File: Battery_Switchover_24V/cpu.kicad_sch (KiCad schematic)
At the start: 54 parts, among them J8 USB_C_Receptacle_USB2.0_14P, M1 Fan, Q1 NPN, SW1 SW_Push, U11 OPA2197xD, U3 LPC11U14FBD48-201, U4 L5973D, U6 AMS1117-3.3, Y1 12.000MHz

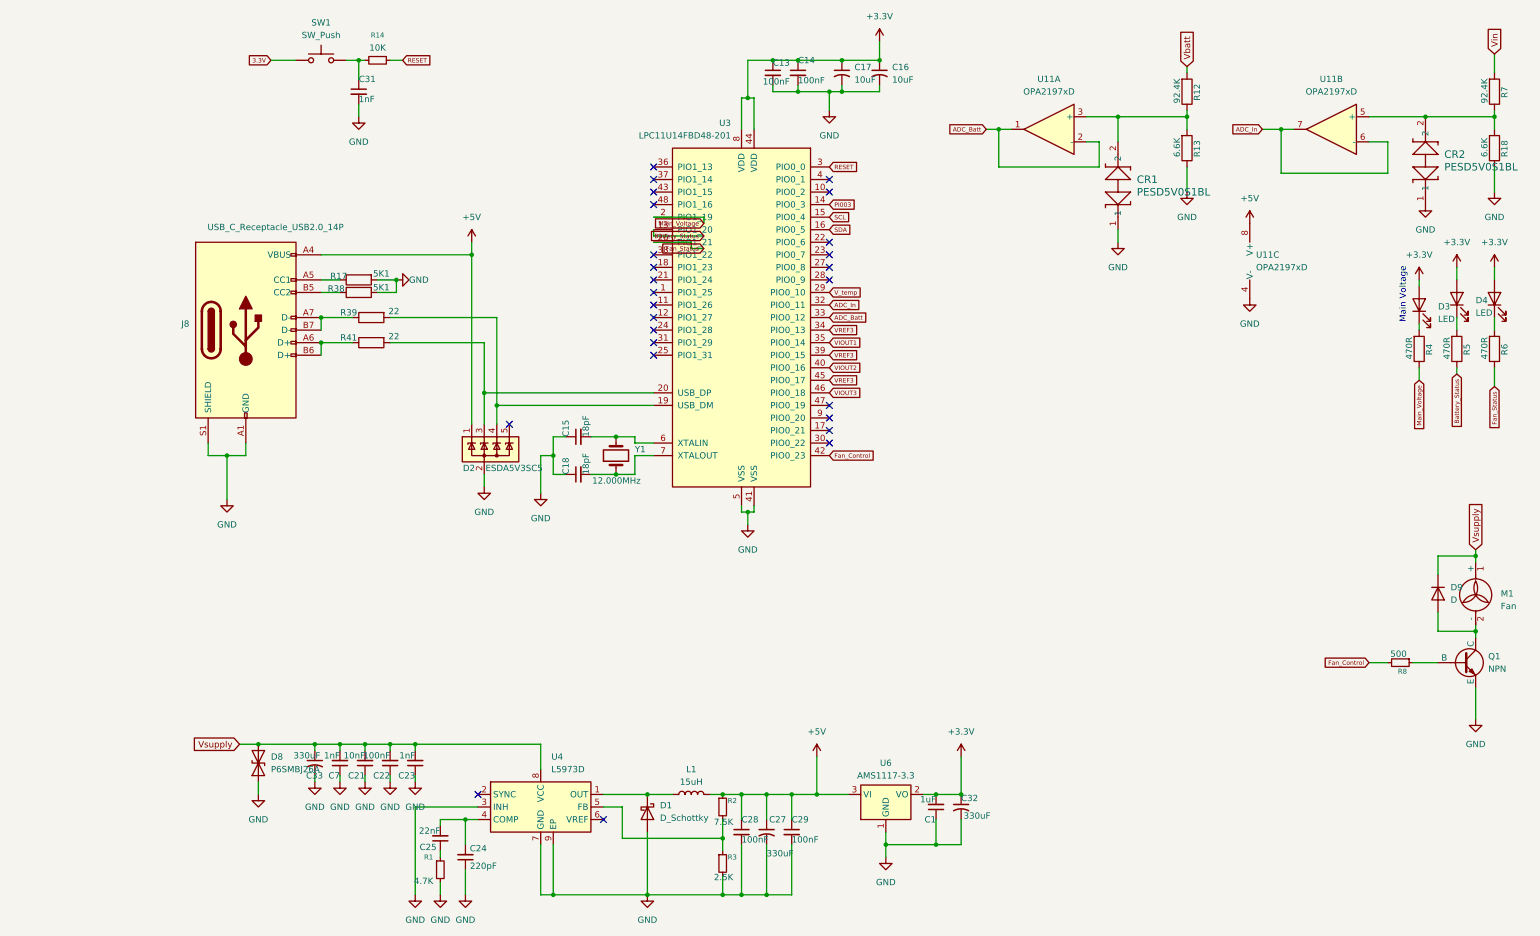
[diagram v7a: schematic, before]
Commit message: Added Some Footprints
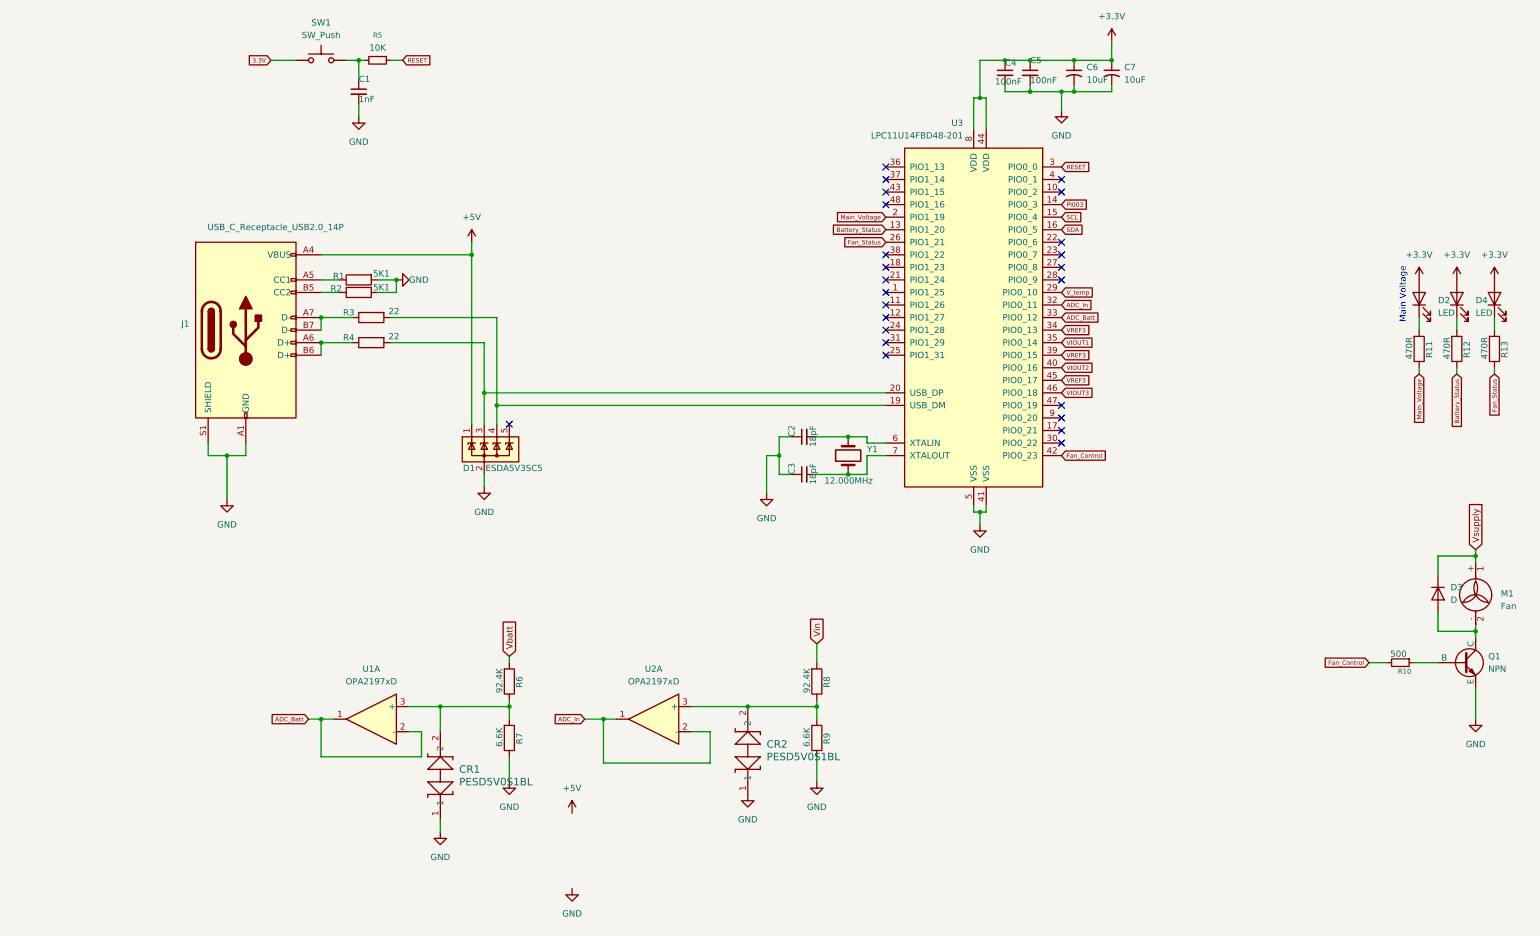
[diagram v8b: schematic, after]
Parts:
- removed C1: 1uF, symbol Device:C_Small
- removed C21: 10nF, symbol Device:C_Small
- removed C22, C28, C29: 100nF, symbol Device:C_Small
- removed C23, C7: 1nF, symbol Device:C_Small
- removed C24: 220pF, symbol Device:C_Small
- removed C25: 22nF, symbol Device:C_Small
- removed C27, C32, C33: 330uF, symbol Device:C_Small_US
- removed D1: D_Schottky, symbol Device:D_Schottky
- removed D8: P6SMBJ26A, symbol Device:D_TVS
- removed L1: 15uH, symbol Device:L
- removed R1: 4.7K, symbol Device:R_Small
- removed R2: 7.5K, symbol Device:R_Small
- removed R3: 2.5K, symbol Device:R_Small
- removed unit 3 of U11
- removed U4: L5973D, Package_SO:HSOP-8-1EP_3.9x4.9mm_P1.27mm_EP2.41x3.1mm_ThermalVias, symbol Regulator_Switching:L5973D
- removed U6: AMS1117-3.3, Package_TO_SOT_SMD:SOT-223-3_TabPin2, symbol Regulator_Linear:AMS1117-3.3
- C1: renamed from C31; footprint (none) -> Capacitor_SMD:C_0603_1608Metric
- C2: renamed from C15; footprint (none) -> Capacitor_SMD:C_0402_1005Metric
- C3: renamed from C18; footprint (none) -> Capacitor_SMD:C_0402_1005Metric
- C4: renamed from C13; footprint (none) -> Capacitor_SMD:C_0603_1608Metric
- C5: renamed from C14; footprint (none) -> Capacitor_SMD:C_0603_1608Metric
- R10: renamed from R8; footprint (none) -> Resistor_SMD:R_0603_1608Metric
- R5: renamed from R14; footprint (none) -> Resistor_SMD:R_0603_1608Metric
- Y1: footprint (none) -> Crystal:Crystal_SMD_HC49-SD
- renumbered C17 to C6, C16 to C7, D2 to D1, D3 to D2, D9 to D3, J8 to J1, R17 to R1, R4 to R11, R5 to R12, R6 to R13, R38 to R2, R39 to R3, R41 to R4, R12 to R6, R13 to R7, R7 to R8, R18 to R9, U11 to U1, U11 to U2
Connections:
- net ADC_In: now also U2.1, U2.2 (-); no longer U2.6 (-), U2.7
- net at CR2.2, R8.1, R9.2: now also U2.3 (+); no longer U2.5 (+)
- no-connect marks 26 -> 24
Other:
- moved on the sheet: C2, C3, C4, C5, C6, C7, CR1, CR2, D2, R6, R7, R8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
